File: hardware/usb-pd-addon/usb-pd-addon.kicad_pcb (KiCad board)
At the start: 2 copper layers, 48 x 40 mm, 51 parts, among them J1 Conn_02x10_Odd_Even, J10 Conn_01x03_Male, J11 Conn_01x03_Male, J12 Conn_01x03_Male, J2 Conn_02x10_Odd_Even, J3 USB_TYPE_C, J4 USB_TYPE_C, J5 Conn_01x03_Male, J6 TPAS, J7 TPBS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

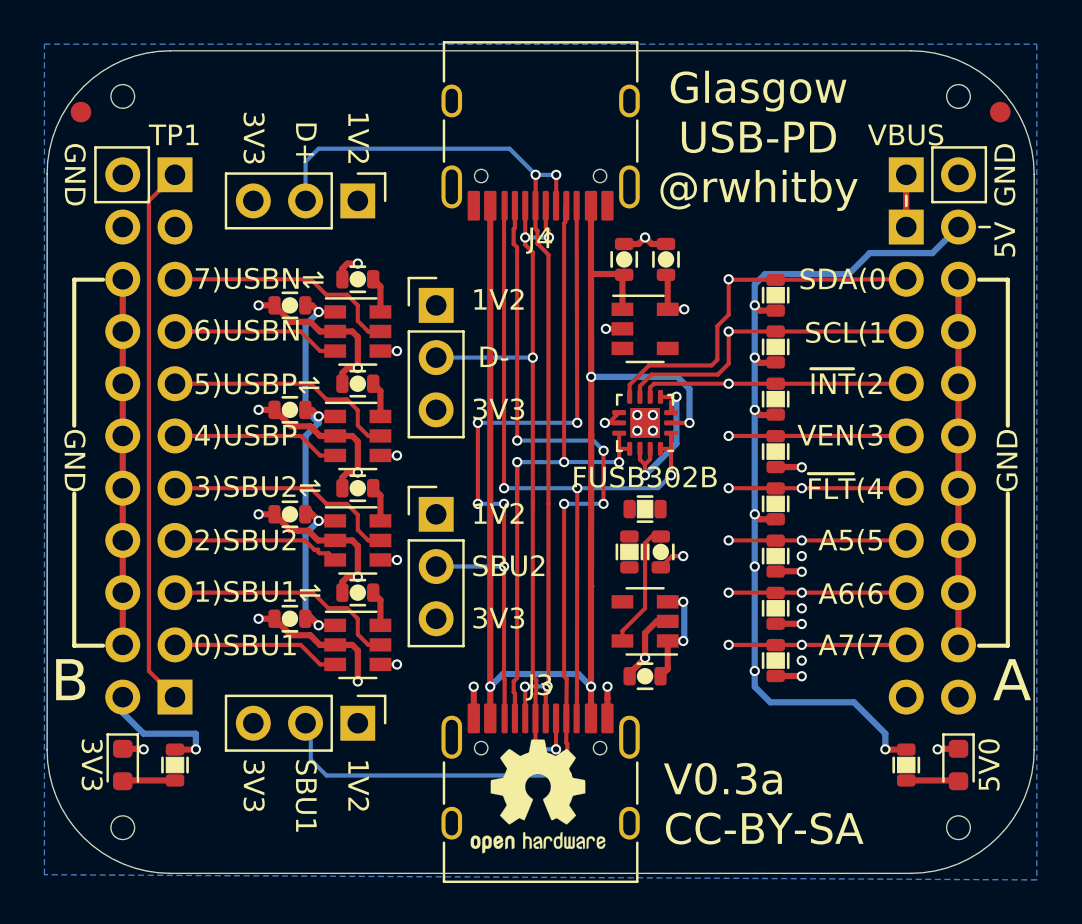
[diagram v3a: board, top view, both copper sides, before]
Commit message: v0.4a: Added decoupling for FUSB302, and protection for DFP mode operation.
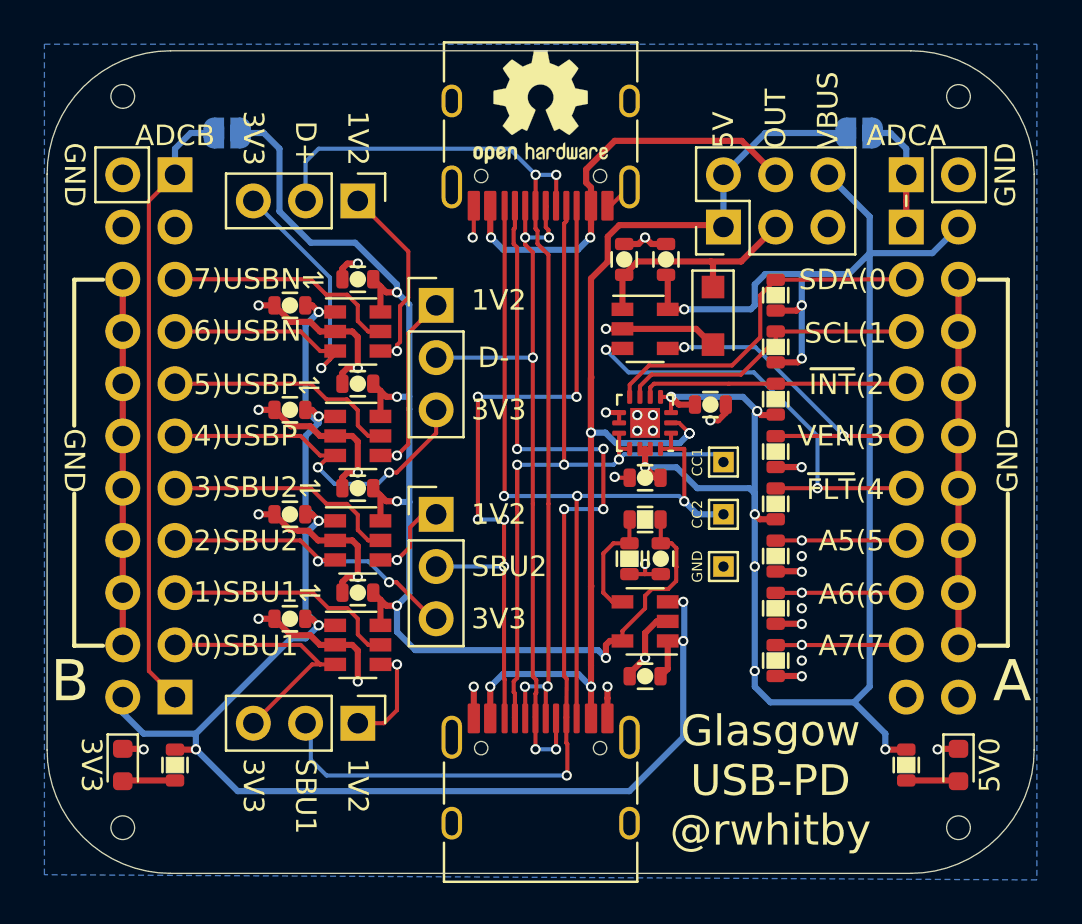
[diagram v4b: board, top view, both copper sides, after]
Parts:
- removed FID1, FID2: Fiducial, Fiducial:Fiducial_1mm_Mask2mm
- added C6: 1uF, pkl_dipol:C_0603, F.Cu at (61.0, 52.8)
- added C8: 0.1u, pkl_dipol:C_0603, F.Cu at (64.1, 49.3)
- added D3: SMF5.0A, Diode_SMD:D_SOD-123F, F.Cu at (64.3, 45.0)
- added J8: Conn_02x03_Odd_Even, Connector_PinHeader_2.54mm:PinHeader_2x03_P2.54mm_Vertical, F.Cu at (64.8, 40.6)
- added JP1: Jumper_2_Open, Jumper:SolderJumper-2_P1.3mm_Open_RoundedPad1.0x1.5mm, B.Cu at (71.4, 36.1)
- added JP2: Jumper_2_Open, Jumper:SolderJumper-2_P1.3mm_Open_RoundedPad1.0x1.5mm, B.Cu at (40.6, 36.1)
- added TP1: TestPoint, TestPoint:TestPoint_THTPad_1.0x1.0mm_Drill0.5mm, F.Cu at (64.8, 52.1)
- added TP2: TestPoint, TestPoint:TestPoint_THTPad_1.0x1.0mm_Drill0.5mm, F.Cu at (64.8, 54.6)
- added TP3: TestPoint, TestPoint:TestPoint_THTPad_1.0x1.0mm_Drill0.5mm, F.Cu at (64.8, 57.1)
- moved LOGO1 33.5 mm to (55.9, 34.8)
- moved LOGO2 33.5 mm to (55.9, 34.8)
- moved R9 0.51 mm to (61.0, 54.9)
- moved C7 0.33 mm to (61.7, 56.8)
- moved R11 0.33 mm to (60.2, 56.8)
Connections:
- C14 pad 1: /VBUS -> /VBUS_DFP
- J2 pad 1: /VBUS -> /AS
- J4 pad A4: /VBUS -> /VBUS_OUT
- J4 pad A9: /VBUS -> /VBUS_OUT
- J4 pad B4: /VBUS -> /VBUS_OUT
- J4 pad B9: /VBUS -> /VBUS_OUT
- J6 pad 1: /VBUS -> /AS
- U2 pad 1: /VBUS -> /VBUS_DFP
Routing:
- net /1.2V: track 13.0 -> 62.3 mm, vias 0 -> 5
- net +3V3: track 35.4 -> 73.9 mm
- net +5V: track 55.0 -> 92.7 mm
- net /VBUS_OUT: track 0.00 -> 21.7 mm, vias 0 -> 2
- net /VBUS: track 68.7 -> 54.9 mm, vias 4 -> 5
- net /~FLT: track 8.64 -> 21.7 mm
- net /VBUS_DFP: track 0.00 -> 11.3 mm
- net GND: track 84.7 -> 95.8 mm, vias 24 -> 27
- net /USBN_3V3: track 8.18 -> 19.1 mm, vias 0 -> 1
- net /USBP_3V3: track 8.18 -> 17.5 mm, vias 0 -> 2
- net /USBN_1V2: track 0.81 -> 9.35 mm
- net /VEN: track 8.64 -> 16.7 mm, vias 1 -> 2
- net /USBP_1V2: track 0.87 -> 8.96 mm
- net /SBU2_3V3: track 8.25 -> 16.0 mm, vias 0 -> 2
- net /AS: track 0.00 -> 5.76 mm
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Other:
- board text added: "1.2V-ADC"
- board text added: "ADCA"
- board text added: "ADCB"
- board text added: "CC1"
- board text added: "CC2"
- board text added: "OUT"
- board text added: "V0.4a CC-BY-SA"
- board text added: "VBUS-ADC"
- board text removed: "TP1"
- board text removed: "V0.3a CC-BY-SA"

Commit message: v0.5a: bulk capacitor for 5V supply and lots of protection added, added more silk.
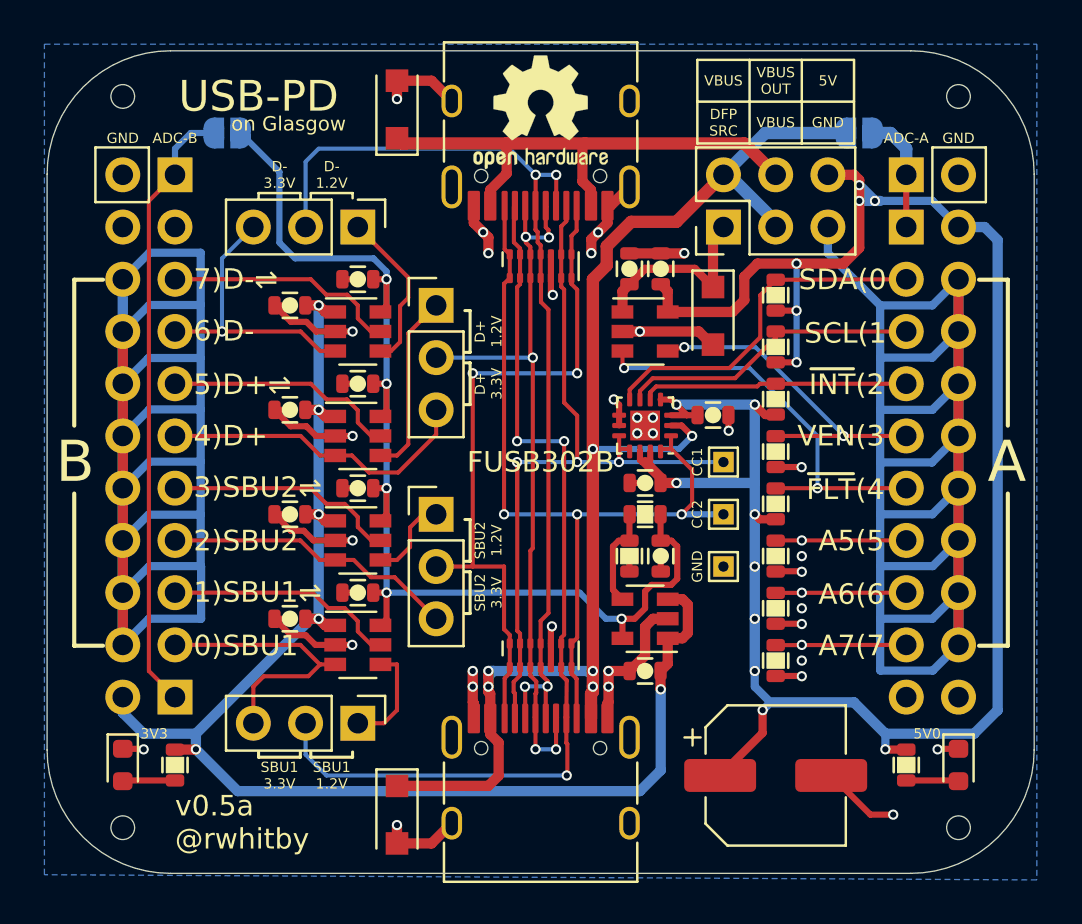
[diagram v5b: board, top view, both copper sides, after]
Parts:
- added C16: 150uF, Capacitor_SMD:CP_Elec_6.3x7.7, F.Cu at (67.3, 67.3)
- added D4: SP3012-06UTG, Glasgow:UDFN-14_3.5x1.35mm_P0.5mm, F.Cu at (55.9, 61.5)
- added D5: SP3012-06UTG, Glasgow:UDFN-14_3.5x1.35mm_P0.5mm, F.Cu at (55.9, 42.5)
- added D6: SMF20A, Diode_SMD:D_SOD-123F, F.Cu at (48.9, 69.2)
- added D7: SMF20A, Diode_SMD:D_SOD-123F, F.Cu at (48.9, 34.9)
- moved J5 1.27 mm to (47.0, 40.6)
- moved C8 0.52 mm to (64.3, 49.8)
- moved C13 0.52 mm to (61.7, 42.7)
- moved C14 0.52 mm to (60.2, 42.7)
- moved C5 0.25 mm to (61.0, 62.2)
- moved C6 0.25 mm to (61.0, 53.1)
- moved LOGO1 0.25 mm to (55.9, 35.1)
- moved LOGO2 0.25 mm to (55.9, 35.1)
- moved R9 0.25 mm to (61.0, 54.6)
- moved U1 0.13 mm to (61.0, 50.3)
- moved U7 0.13 mm to (61.0, 59.7)
- moved C7 0.13 mm to (61.7, 56.6)
- moved R11 0.13 mm to (60.2, 56.6)
- moved U2 0.13 mm to (61.0, 45.7)
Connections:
- J8 pad 1: /VBUS -> /VBUS_DFP
- J8 pad 3: /VBUS_DFP -> /VBUS
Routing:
- net GND: track 95.8 -> 247.3 mm, vias 27 -> 42
- net +5V: track 92.7 -> 106.8 mm, vias 10 -> 15
- net /VBUS: track 54.9 -> 64.8 mm, vias 5 -> 6
- net /USBN_3V3: track 19.1 -> 14.0 mm
- net /1.2V: track 62.3 -> 57.7 mm
- net /VBUS_OUT: track 21.7 -> 25.8 mm, vias 2 -> 0
- net /SBU1: track 48.7 -> 45.2 mm, vias 5 -> 3
- net +3V3: track 73.9 -> 70.4 mm, vias 7 -> 6
- net /VBUS_DFP: track 11.3 -> 9.36 mm
- net /USBP_3V3: track 17.5 -> 15.7 mm, vias 2 -> 0
- net /USBN: track 45.9 -> 47.5 mm
- net /SBU2_3V3: track 16.0 -> 14.4 mm, vias 2 -> 0
- net /USBN_1V2: track 9.35 -> 7.91 mm, vias 1 -> 0
- net /~FLT: track 21.7 -> 20.5 mm
- net /SBU1_3V3: track 12.6 -> 13.7 mm
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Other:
- board text added: "4)D+"
- board text added: "5)D+⇌"
- board text added: "6)D-"
- board text added: "7)D-⇌"
- board text added: "ADC-A"
- board text added: "ADC-B"
- board text added: "ADC-VBUS"
- board text added: "D+ 1.2V"
- board text added: "D+ 3.3V"
- board text added: "D+(4"
- board text added: "D+⇌(5"
- board text added: "D- 1.2V"
- board text added: "D- 3.3V"
- board text added: "D-(6"
- board text added: "D-⇌(7"
- board text added: "DFP SRC"
- board text added: "SBU1 1.2V"
- board text added: "SBU1 3.3V"
- board text added: "SBU2 1.2V"
- board text added: "SBU2 3.3V"
- board text added: "USB-PD"
- board text added: "VBUS OUT"
- board text added: "on Glasgow"
- board text added: "v0.5a @rwhitby"
- board text added: "v0.5a CC-BY-SA"
- board text removed: "1V2"
- board text removed: "4)USBP"
- board text removed: "5)USBP⇌"
- board text removed: "6)USBN"
- board text removed: "7)USBN⇌"
- board text removed: "ADCA"
- board text removed: "ADCB"
- board text removed: "D+"
- board text removed: "D-"
- board text removed: "OUT"
- board text removed: "SBU1"
- board text removed: "SBU2"
- board text removed: "USBN(6"
- board text removed: "USBN⇌(7"
- board text removed: "USBP(4"
- board text removed: "USBP⇌(5"
- board text removed: "V0.4a CC-BY-SA"
- board text removed: "VBUS-ADC"

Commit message: v0.6a: Changed to 4 layer board, added caps on CC1/CC2, squared top edge of board, increased silk legibility.
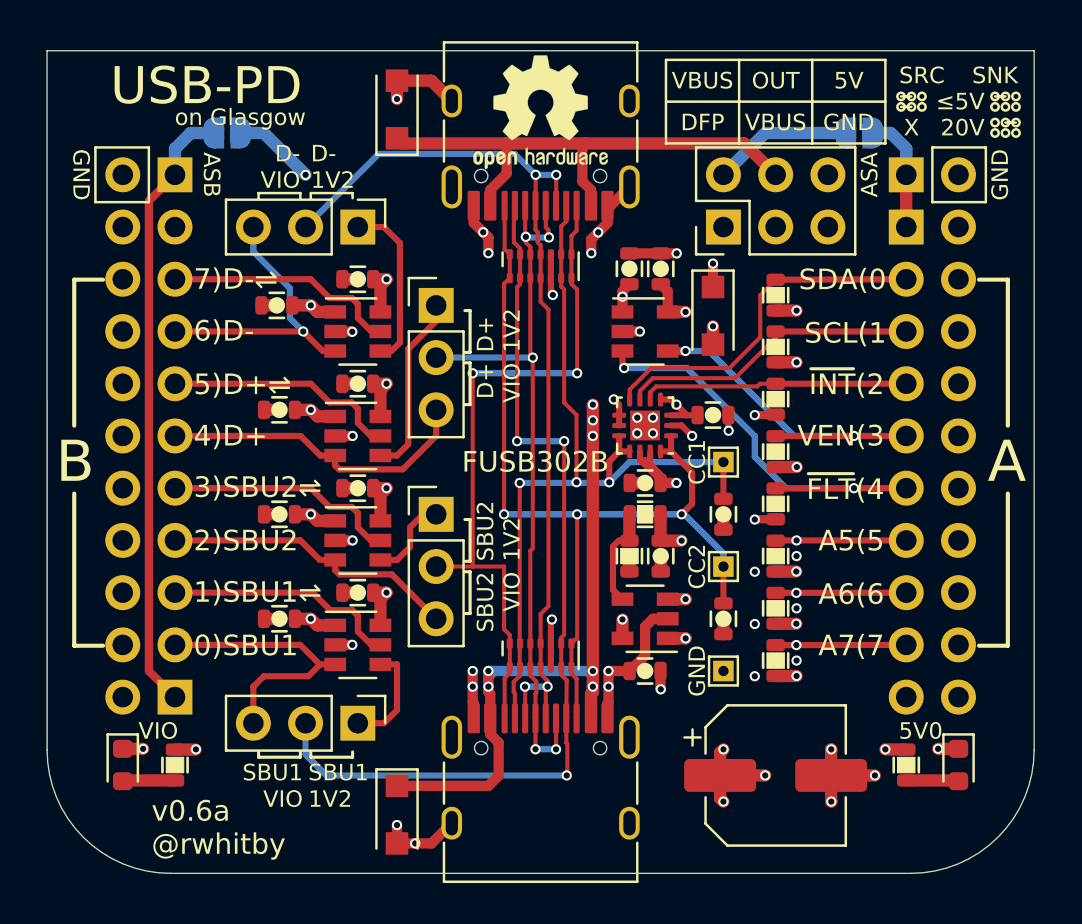
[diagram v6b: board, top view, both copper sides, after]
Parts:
- removed TH1, TH2, TH3, TH4: Mounting_Hole, pkl_pads:ToolingHole
- added C15: 200pF, pkl_dipol:C_0603, F.Cu at (64.8, 54.6)
- added C17: 200pF, pkl_dipol:C_0603, F.Cu at (64.8, 59.7)
- moved TP3 5.08 mm to (64.8, 62.2)
- moved TP2 2.54 mm to (64.8, 57.1)
- moved C1 0.64 mm to (43.1, 44.5)
- moved C10 0.51 mm to (43.2, 59.7)
- moved C2 0.51 mm to (43.2, 54.6)
- moved C9 0.51 mm to (43.2, 49.5)
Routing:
- net GND: track 247.3 -> 201.6 mm, vias 42 -> 48
- net /VBUS: track 64.8 -> 73.1 mm, vias 6 -> 8
- net +5V: track 106.8 -> 114.4 mm, vias 15 -> 14
- net +3V3: track 70.4 -> 65.9 mm, vias 6 -> 8
- net /CC2: track 41.0 -> 44.2 mm
- net /USBN: track 47.5 -> 45.3 mm
- net /1.2V: track 57.7 -> 59.2 mm, vias 5 -> 7
- net /~FLT: track 20.5 -> 21.4 mm
- net /CC1: track 39.8 -> 40.6 mm
- net /VBUS_DFP: track 9.36 -> 9.68 mm, vias 0 -> 2
- added copper zone on In2.Cu, net +3V3
- added copper zone on In2.Cu, net +5V
- added copper zone on In2.Cu, net /1.2V
- added copper zone on In2.Cu, net /VBUS
- added copper zone on In2.Cu, net /VBUS_DFP
- added copper zone on In1.Cu, net GND
- removed copper zone on B.Cu, net GND
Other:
- outline, holes or cut-outs redrawn
- copper layers 2 -> 4
- board text added: "20V"
- board text added: "ASA"
- board text added: "ASB"
- board text added: "D+ 1V2"
- board text added: "D+ VIO"
- board text added: "D- 1V2"
- board text added: "D- VIO"
- board text added: "DFP"
- board text added: "OUT"
- board text added: "SBU1 1V2"
- board text added: "SBU1 VIO"
- board text added: "SBU2 1V2"
- board text added: "SBU2 VIO"
- board text added: "SNK"
- board text added: "SRC"
- board text added: "VIO"
- board text added: "X"
- board text added: "v0.6a @rwhitby"
- board text added: "v0.6a CC-BY-SA"
- board text added: "≤5V"
- board text removed: "3V3"
- board text removed: "ADC-A"
- board text removed: "ADC-B"
- board text removed: "D+ 1.2V"
- board text removed: "D+ 3.3V"
- board text removed: "D- 1.2V"
- board text removed: "D- 3.3V"
- board text removed: "DFP SRC"
- board text removed: "SBU1 1.2V"
- board text removed: "SBU1 3.3V"
- board text removed: "SBU2 1.2V"
- board text removed: "SBU2 3.3V"
- board text removed: "VBUS OUT"
- board text removed: "v0.5a @rwhitby"
- board text removed: "v0.5a CC-BY-SA"
